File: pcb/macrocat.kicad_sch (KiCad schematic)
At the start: 52 parts

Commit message: finish pcb layout
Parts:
- C1, C2, C3, C4, C5, C6, C7: renamed from C?; footprint (none) -> Capacitor_SMD:C_0805_2012Metric
- F1: renamed from F?; footprint (none) -> Fuse:Fuse_1206_3216Metric
- MX1, MX10, MX11, MX12, MX13, MX14, MX15, MX16, MX2, MX3, MX4, MX5, MX6, MX7, MX8, MX9: renamed from MX?; footprint (none) -> MX_Only:MXOnly-1U-Hotswap
- OL1: renamed from OL?; footprint (none) -> kbd:OLED_v2
- R1, R2, R4, R5, R6: renamed from R?; footprint (none) -> Resistor_SMD:R_0805_2012Metric
- R3: renamed from R?; value R_Small -> 10k; footprint (none) -> Resistor_SMD:R_0805_2012Metric
- SW1: renamed from SW?; footprint (none) -> Button_Switch_SMD:SW_DIP_SPSTx01_Slide_6.7x4.1mm_W6.73mm_P2.54mm_LowProfile_JPin
- SW2: renamed from SW?; footprint (none) -> Rotary_Encoder:RotaryEncoder_Alps_EC11E-Switch_Vertical_H20mm
- Y1: renamed from Y?; footprint (none) -> Crystal:Crystal_SMD_3225-4Pin_3.2x2.5mm
- gave numbers to parts that had none: 18
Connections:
- net COL1: now also U1.29 (PB5); no longer U1.8 (PB0)
- net COL2: now also U1.30 (PB6); no longer U1.9 (PB1)
- net COL3: now also U1.31 (PC6); no longer U1.10 (PB2)
- net COL4: now also U1.32 (PC7); no longer U1.11 (PB3)
- net KNOB1: now also U1.20 (PD2)
- net KNOB2: now also U1.21 (PD3)
- net ROW1: now also U1.25 (PD4); no longer U1.28 (PB4)
- net ROW2: now also U1.26 (PD6); no longer U1.29 (PB5)
- net ROW3: now also U1.27 (PD7); no longer U1.30 (PB6)
- net ROW4: now also U1.28 (PB4); no longer U1.12 (PB7)
- net SCL: now also U1.18 (PD0)
- net SDA: now also U1.19 (PD1)

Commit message: adjust some figures on pcb
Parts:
- J1: value USB-C USB 2.0 MC-372 -> USB-C Connector
- Y1: value Crystal_GND24_Small -> 16M
- renumbered SW2 to KNOB1, SW1 to RESET1
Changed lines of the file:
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@@
   (symbol (lib_id "Device:RotaryEncoder_Switch") (at 124.46 100.33 0) (unit 1)
     (in_bom yes) (on_board yes) (fields_autoplaced)
-    (property "Reference" "SW2" (id 0) (at 124.46 90.17 0))
+    (property "Reference" "KNOB1" (id 0) (at 124.46 90.17 0))
     (property "Value" "RotaryEncoder_Switch" (id 1) (at 124.46 92.71 0))
     (property "Footprint" "Rotary_Encoder:RotaryEncoder_Alps_EC11E-Switch_Vertical_H20mm" (id 2) (at 120.65 96.266 0)
@@
   (symbol (lib_id "Switch:SW_Push") (at 40.64 36.83 0) (unit 1)
     (in_bom yes) (on_board yes) (fields_autoplaced)
-    (property "Reference" "SW1" (id 0) (at 40.64 29.21 0))
+    (property "Reference" "RESET1" (id 0) (at 40.64 29.21 0))
     (property "Value" "SW_Push" (id 1) (at 40.64 31.75 0))
     (property "Footprint" "Button_Switch_SMD:SW_DIP_SPSTx01_Slide_6.7x4.1mm_W6.73mm_P2.54mm_LowProfile_JPin" (id 2) (at 40.64 31.75 0)
@@
   (symbol (lib_id "Device:Crystal_GND24_Small") (at 38.1 44.45 90) (unit 1)
     (in_bom yes) (on_board yes) (fields_autoplaced)
-    (property "Reference" "Y1" (id 0) (at 52.07 39.751 90))
-    (property "Value" "Crystal_GND24_Small" (id 1) (at 52.07 42.291 90))
+    (property "Reference" "Y1" (id 0) (at 43.18 39.751 90))
+    (property "Value" "16M" (id 1) (at 43.18 42.291 90))
     (property "Footprint" "Crystal:Crystal_SMD_3225-4Pin_3.2x2.5mm" (id 2) (at 38.1 44.45 0)
       (effects (font (size 1.27 1.27)) hide)
@@
     (in_bom yes) (on_board yes)
     (property "Reference" "J1" (id 0) (at 132.2578 26.4922 0))
-    (property "Value" "USB-C USB 2.0 MC-372" (id 1) (at 132.2578 28.8036 0))
+    (property "Value" "USB-C Connector" (id 1) (at 132.2578 28.8036 0))
     (property "Footprint" "nrfmicro:USB-C_C168688" (id 2) (at 132.2578 31.115 0))
     (property "Datasheet" "https://www.usb.org/sites/default/files/documents/usb_type-c.zip" (id 3) (at 133.35 50.8 0)
@@
     )
     (path "/eb46497f-7da4-4d09-b0bc-ff28c911e659"
-      (reference "J1") (unit 1) (value "USB-C USB 2.0 MC-372") (footprint "nrfmicro:USB-C_C168688")
+      (reference "J1") (unit 1) (value "USB-C Connector") (footprint "nrfmicro:USB-C_C168688")
+    )
+    (path "/7ce1fa23-e6c8-4f4d-a700-97b0bc833646"
+      (reference "KNOB1") (unit 1) (value "RotaryEncoder_Switch") (footprint "Rotary_Encoder:RotaryEncoder_Alps_EC11E-Switch_Vertical_H20mm")
     )
     (path "/4dc965b4-2750-4e34-ac33-80b79bca93bb"
@@
     )
     (path "/9522c7ba-7f5c-4bf1-bcc9-9822f7337371"
-      (reference "SW1") (unit 1) (value "SW_Push") (footprint "Button_Switch_SMD:SW_DIP_SPSTx01_Slide_6.7x4.1mm_W6.73mm_P2.54mm_LowProfile_JPin")
-    )
-    (path "/7ce1fa23-e6c8-4f4d-a700-97b0bc833646"
-      (reference "SW2") (unit 1) (value "RotaryEncoder_Switch") (footprint "Rotary_Encoder:RotaryEncoder_Alps_EC11E-Switch_Vertical_H20mm")
+      (reference "RESET1") (unit 1) (value "SW_Push") (footprint "Button_Switch_SMD:SW_DIP_SPSTx01_Slide_6.7x4.1mm_W6.73mm_P2.54mm_LowProfile_JPin")
     )
     (path "/30fb2a30-8a24-4b31-9ec0-7dad9c08990b"
@@
     )
     (path "/de1b2933-e9ed-4629-ac8a-93e96f4f2a1f"
-      (reference "Y1") (unit 1) (value "Crystal_GND24_Small") (footprint "Crystal:Crystal_SMD_3225-4Pin_3.2x2.5mm")
-    )
-  )
+      (reference "Y1") (unit 1) (value "16M") (footprint "Crystal:Crystal_SMD_3225-4Pin_3.2x2.5mm")
+    )
+  )

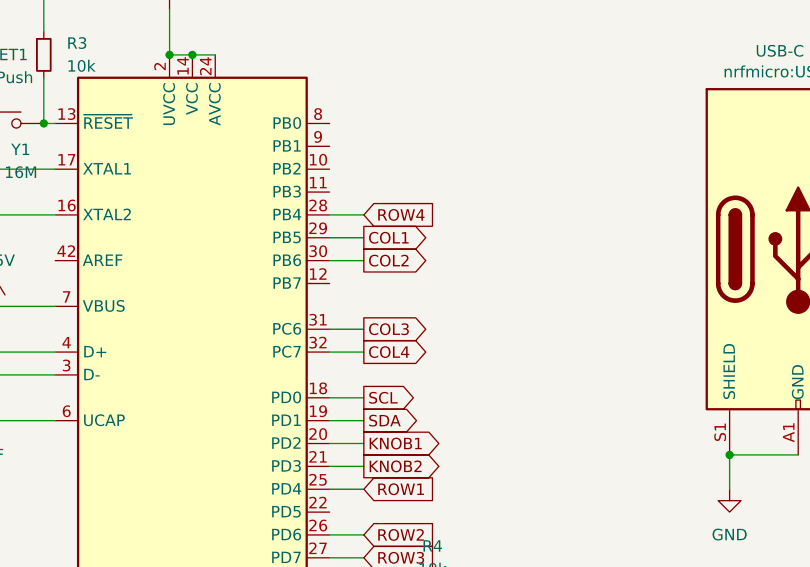
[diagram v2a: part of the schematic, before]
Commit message: optimize mcu part wiring
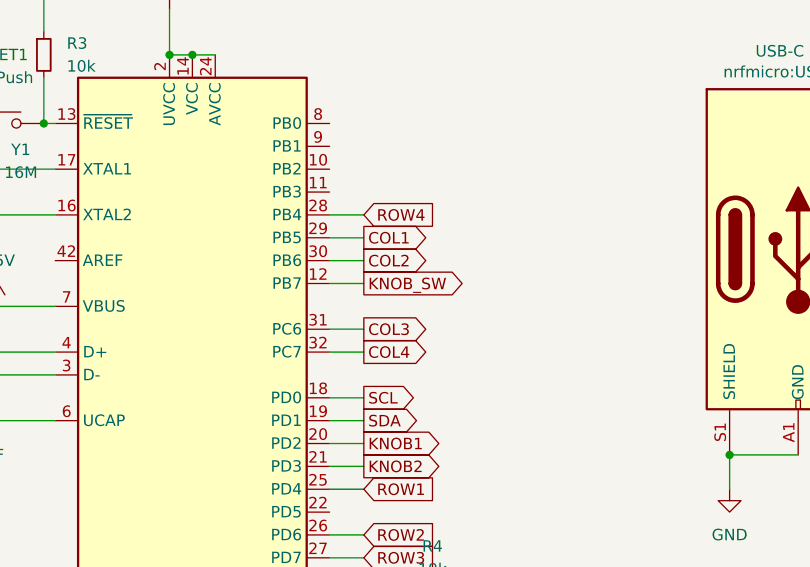
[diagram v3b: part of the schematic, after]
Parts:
- D1, D10, D11, D12, D13, D14, D15, D16, D2, D3, D4, D5, D6, D7, D8, D9: footprint Diode_SMD:D_SOD-123 -> macrocat:D_SOD-123_back
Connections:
- net KNOB_SW: now also U1.12 (PB7)
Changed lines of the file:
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@@
+    (stroke (width 0) (type default) (color 0 0 0 0))
+  )
+  (wire (pts (xy 77.47 54.61) (xy 81.28 54.61))
     (stroke (width 0) (type default) (color 0 0 0 0))
   )
@@
     )
   )
+  (global_label "KNOB_SW" (shape output) (at 81.28 54.61 0) (fields_autoplaced)
+    (effects (font (size 1.27 1.27)) (justify left))
+    (property "Intersheet References" "${INTERSHEET_REFS}" (id 0) (at 92.5226 54.5306 0)
+      (effects (font (size 1.27 1.27)) (justify left) hide)
+    )
+  )
   (global_label "ROW4" (shape input) (at 81.28 46.99 0) (fields_autoplaced)
     (effects (font (size 1.27 1.27)) (justify left))
@@
       (effects (font (size 1.27 1.27)) (justify right))
     )
-    (property "Footprint" "Diode_SMD:D_SOD-123" (id 2) (at 219.075 77.47 0)
+    (property "Footprint" "macrocat:D_SOD-123_back" (id 2) (at 219.075 77.47 0)
       (effects (font (size 1.27 1.27)) hide)
     )
@@
       (effects (font (size 1.27 1.27)) (justify right))
     )
-    (property "Footprint" "Diode_SMD:D_SOD-123" (id 2) (at 191.135 120.65 0)
+    (property "Footprint" "macrocat:D_SOD-123_back" (id 2) (at 191.135 120.65 0)
       (effects (font (size 1.27 1.27)) hide)
     )
@@
       (effects (font (size 1.27 1.27)) (justify right))
     )
-    (property "Footprint" "Diode_SMD:D_SOD-123" (id 2) (at 219.075 99.06 0)
+    (property "Footprint" "macrocat:D_SOD-123_back" (id 2) (at 219.075 99.06 0)
       (effects (font (size 1.27 1.27)) hide)
     )
@@
       (effects (font (size 1.27 1.27)) (justify right))
     )
-    (property "Footprint" "Diode_SMD:D_SOD-123" (id 2) (at 219.075 142.24 0)
+    (property "Footprint" "macrocat:D_SOD-123_back" (id 2) (at 219.075 142.24 0)
       (effects (font (size 1.27 1.27)) hide)
     )
@@
       (effects (font (size 1.27 1.27)) (justify right))
     )
-    (property "Footprint" "Diode_SMD:D_SOD-123" (id 2) (at 219.075 120.65 0)
+    (property "Footprint" "macrocat:D_SOD-123_back" (id 2) (at 219.075 120.65 0)
       (effects (font (size 1.27 1.27)) hide)
     )
@@
       (effects (font (size 1.27 1.27)) (justify right))
     )
-    (property "Footprint" "Diode_SMD:D_SOD-123" (id 2) (at 191.135 77.47 0)
+    (property "Footprint" "macrocat:D_SOD-123_back" (id 2) (at 191.135 77.47 0)
       (effects (font (size 1.27 1.27)) hide)
     )
@@
       (effects (font (size 1.27 1.27)) (justify right))
     )
-    (property "Footprint" "Diode_SMD:D_SOD-123" (id 2) (at 175.895 142.24 0)
+    (property "Footprint" "macrocat:D_SOD-123_back" (id 2) (at 175.895 142.24 0)
       (effects (font (size 1.27 1.27)) hide)
     )
@@
       (effects (font (size 1.27 1.27)) (justify right))
     )
-    (property "Footprint" "Diode_SMD:D_SOD-123" (id 2) (at 205.105 142.24 0)
+    (property "Footprint" "macrocat:D_SOD-123_back" (id 2) (at 205.105 142.24 0)
       (effects (font (size 1.27 1.27)) hide)
     )
@@
       (effects (font (size 1.27 1.27)) (justify right))
     )
-    (property "Footprint" "Diode_SMD:D_SOD-123" (id 2) (at 191.135 142.24 0)
+    (property "Footprint" "macrocat:D_SOD-123_back" (id 2) (at 191.135 142.24 0)
       (effects (font (size 1.27 1.27)) hide)
     )
@@
       (effects (font (size 1.27 1.27)) (justify right))
     )
-    (property "Footprint" "Diode_SMD:D_SOD-123" (id 2) (at 205.105 77.47 0)
+    (property "Footprint" "macrocat:D_SOD-123_back" (id 2) (at 205.105 77.47 0)
       (effects (font (size 1.27 1.27)) hide)
     )
@@
       (effects (font (size 1.27 1.27)) (justify right))
     )
-    (property "Footprint" "Diode_SMD:D_SOD-123" (id 2) (at 175.895 120.65 0)
+    (property "Footprint" "macrocat:D_SOD-123_back" (id 2) (at 175.895 120.65 0)
       (effects (font (size 1.27 1.27)) hide)
     )
@@
       (effects (font (size 1.27 1.27)) (justify right))
     )
-    (property "Footprint" "Diode_SMD:D_SOD-123" (id 2) (at 191.135 99.06 0)
+    (property "Footprint" "macrocat:D_SOD-123_back" (id 2) (at 191.135 99.06 0)
       (effects (font (size 1.27 1.27)) hide)
     )
@@
       (effects (font (size 1.27 1.27)) (justify right))
     )
-    (property "Footprint" "Diode_SMD:D_SOD-123" (id 2) (at 205.105 99.06 0)
+    (property "Footprint" "macrocat:D_SOD-123_back" (id 2) (at 205.105 99.06 0)
       (effects (font (size 1.27 1.27)) hide)
     )
@@
       (effects (font (size 1.27 1.27)) (justify right))
     )
-    (property "Footprint" "Diode_SMD:D_SOD-123" (id 2) (at 175.895 77.47 0)
+    (property "Footprint" "macrocat:D_SOD-123_back" (id 2) (at 175.895 77.47 0)
       (effects (font (size 1.27 1.27)) hide)
     )
@@
       (effects (font (size 1.27 1.27)) (justify right))
     )
-    (property "Footprint" "Diode_SMD:D_SOD-123" (id 2) (at 175.895 99.06 0)
+    (property "Footprint" "macrocat:D_SOD-123_back" (id 2) (at 175.895 99.06 0)
       (effects (font (size 1.27 1.27)) hide)
     )
@@
       (effects (font (size 1.27 1.27)) (justify right))
     )
-    (property "Footprint" "Diode_SMD:D_SOD-123" (id 2) (at 205.105 120.65 0)
+    (property "Footprint" "macrocat:D_SOD-123_back" (id 2) (at 205.105 120.65 0)
       (effects (font (size 1.27 1.27)) hide)
     )
@@
     )
     (path "/ed28ec15-b0c4-429e-bfb5-1090db56b039"
-      (reference "D1") (unit 1) (value "1N4148W") (footprint "Diode_SMD:D_SOD-123")
+      (reference "D1") (unit 1) (value "1N4148W") (footprint "macrocat:D_SOD-123_back")
     )
     (path "/f68676dc-ae8e-4c00-8d23-f2622b476285"
-      (reference "D2") (unit 1) (value "1N4148W") (footprint "Diode_SMD:D_SOD-123")
+      (reference "D2") (unit 1) (value "1N4148W") (footprint "macrocat:D_SOD-123_back")
     )
     (path "/9f999266-b7b0-4046-9886-c36d3812d8b9"
-      (reference "D3") (unit 1) (value "1N4148W") (footprint "Diode_SMD:D_SOD-123")
+      (reference "D3") (unit 1) (value "1N4148W") (footprint "macrocat:D_SOD-123_back")
     )
     (path "/33dd56e8-4348-4ca6-b993-ce803080e9f9"
-      (reference "D4") (unit 1) (value "1N4148W") (footprint "Diode_SMD:D_SOD-123")
+      (reference "D4") (unit 1) (value "1N4148W") (footprint "macrocat:D_SOD-123_back")
     )
     (path "/326caa68-27e4-4157-bd61-b64e90feefa0"
-      (reference "D5") (unit 1) (value "1N4148W") (footprint "Diode_SMD:D_SOD-123")
+      (reference "D5") (unit 1) (value "1N4148W") (footprint "macrocat:D_SOD-123_back")
     )
     (path "/bfcf114a-2d07-459e-aff0-f58915bf150d"
-      (reference "D6") (unit 1) (value "1N4148W") (footprint "Diode_SMD:D_SOD-123")
+      (reference "D6") (unit 1) (value "1N4148W") (footprint "macrocat:D_SOD-123_back")
     )
     (path "/0a594385-bc6f-482e-924b-efbe02ea92bd"
-      (reference "D7") (unit 1) (value "1N4148W") (footprint "Diode_SMD:D_SOD-123")
+      (reference "D7") (unit 1) (value "1N4148W") (footprint "macrocat:D_SOD-123_back")
     )
     (path "/585c8182-3940-44d9-839d-035c52844dc8"
-      (reference "D8") (unit 1) (value "1N4148W") (footprint "Diode_SMD:D_SOD-123")
+      (reference "D8") (unit 1) (value "1N4148W") (footprint "macrocat:D_SOD-123_back")
     )
     (path "/7db0e24b-f3df-46f7-a725-017655a8ac3f"
-      (reference "D9") (unit 1) (value "1N4148W") (footprint "Diode_SMD:D_SOD-123")
+      (reference "D9") (unit 1) (value "1N4148W") (footprint "macrocat:D_SOD-123_back")
     )
     (path "/db271fd7-5bdb-40a6-816e-5685369254ee"
-      (reference "D10") (unit 1) (value "1N4148W") (footprint "Diode_SMD:D_SOD-123")
+      (reference "D10") (unit 1) (value "1N4148W") (footprint "macrocat:D_SOD-123_back")
     )
     (path "/ff3fe538-02e5-4c3d-8a20-2913066953d2"
-      (reference "D11") (unit 1) (value "1N4148W") (footprint "Diode_SMD:D_SOD-123")
+      (reference "D11") (unit 1) (value "1N4148W") (footprint "macrocat:D_SOD-123_back")
     )
     (path "/4f700c09-4274-4ff1-a146-e39efa03c114"
-      (reference "D12") (unit 1) (value "1N4148W") (footprint "Diode_SMD:D_SOD-123")
+      (reference "D12") (unit 1) (value "1N4148W") (footprint "macrocat:D_SOD-123_back")
     )
     (path "/056c19b5-c8f4-44c6-a068-8944b943ef81"
-      (reference "D13") (unit 1) (value "1N4148W") (footprint "Diode_SMD:D_SOD-123")
+      (reference "D13") (unit 1) (value "1N4148W") (footprint "macrocat:D_SOD-123_back")
     )
     (path "/1ec876c6-2620-4b42-9759-66915cae0137"
-      (reference "D14") (unit 1) (value "1N4148W") (footprint "Diode_SMD:D_SOD-123")
+      (reference "D14") (unit 1) (value "1N4148W") (footprint "macrocat:D_SOD-123_back")
     )
     (path "/2c92c5e1-236f-4fae-9058-40ed9bc9a0ed"
-      (reference "D15") (unit 1) (value "1N4148W") (footprint "Diode_SMD:D_SOD-123")
+      (reference "D15") (unit 1) (value "1N4148W") (footprint "macrocat:D_SOD-123_back")
     )
     (path "/202d6bb7-f690-4b44-b9f8-5c82ff8d8a7d"
-      (reference "D16") (unit 1) (value "1N4148W") (footprint "Diode_SMD:D_SOD-123")
+      (reference "D16") (unit 1) (value "1N4148W") (footprint "macrocat:D_SOD-123_back")
     )
     (path "/4632957c-a340-4ebd-9ec7-29b9907640f8"

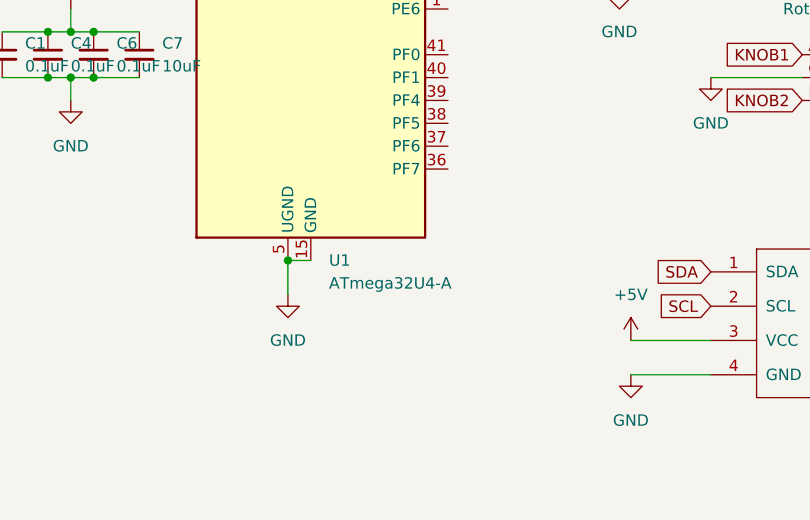
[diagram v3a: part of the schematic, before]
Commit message: change mcu to atmega32u4-mu
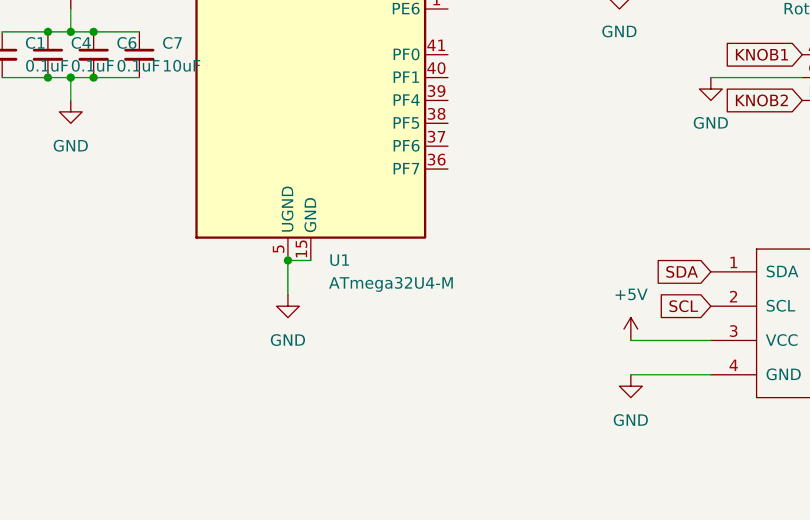
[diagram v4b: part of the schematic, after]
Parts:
- U1: value ATmega32U4-A -> ATmega32U4-M; footprint Package_QFP:TQFP-44_10x10mm_P0.8mm -> Package_DFN_QFN:QFN-44-1EP_7x7mm_P0.5mm_EP5.2x5.2mm; symbol MCU_Microchip_ATmega:ATmega32U4-A -> MCU_Microchip_ATmega:ATmega32U4-M
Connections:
- net GND: now also U1.45 (GND)
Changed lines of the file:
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@@
     (pin "2")
   )
-  (symbol (lib_id "MCU_Microchip_ATmega:ATmega32U4-A") (at 62.23 74.93 0) (unit 1)
+  (symbol (lib_id "MCU_Microchip_ATmega:ATmega32U4-M") (at 62.23 74.93 0) (unit 1)
     (in_bom yes) (on_board yes) (fields_autoplaced)
     (property "Reference" "U1" (id 0) (at 64.2494 120.65 0)
       (effects (font (size 1.27 1.27)) (justify left))
     )
-    (property "Value" "ATmega32U4-A" (id 1) (at 64.2494 123.19 0)
+    (property "Value" "ATmega32U4-M" (id 1) (at 64.2494 123.19 0)
       (effects (font (size 1.27 1.27)) (justify left))
     )
-    (property "Footprint" "Package_QFP:TQFP-44_10x10mm_P0.8mm" (id 2) (at 62.23 74.93 0)
+    (property "Footprint" "Package_DFN_QFN:QFN-44-1EP_7x7mm_P0.5mm_EP5.2x5.2mm" (id 2) (at 62.23 74.93 0)
       (effects (font (size 1.27 1.27) italic) hide)
     )
@@
     (pin "43")
     (pin "44")
+    (pin "45")
     (pin "5")
     (pin "6")
@@
     )
     (path "/30fb2a30-8a24-4b31-9ec0-7dad9c08990b"
-      (reference "U1") (unit 1) (value "ATmega32U4-A") (footprint "Package_QFP:TQFP-44_10x10mm_P0.8mm")
+      (reference "U1") (unit 1) (value "ATmega32U4-M") (footprint "Package_DFN_QFN:QFN-44-1EP_7x7mm_P0.5mm_EP5.2x5.2mm")
     )
     (path "/de1b2933-e9ed-4629-ac8a-93e96f4f2a1f"
